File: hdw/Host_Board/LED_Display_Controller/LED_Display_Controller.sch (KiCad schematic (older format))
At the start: 0 parts

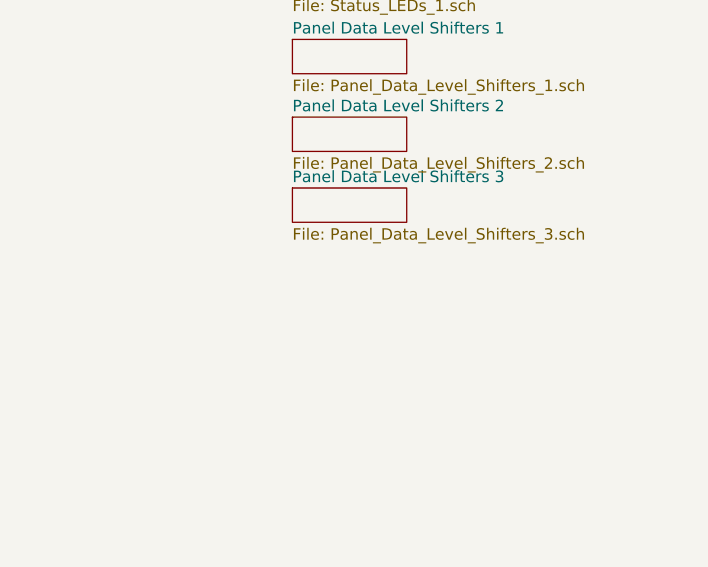
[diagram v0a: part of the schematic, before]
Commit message: Added test points sheet
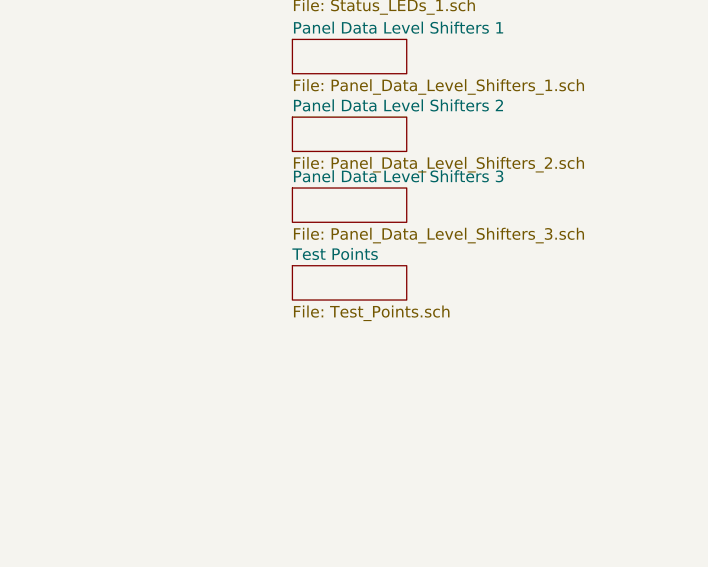
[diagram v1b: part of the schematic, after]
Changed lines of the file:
@@
 $Descr A 11000 8500
 encoding utf-8
-Sheet 1 25
+Sheet 1 26
 Title ""
 Date ""
@@
 Text Notes 710  7660 0    50   ~ 0
 To Do List:\n* Add +5V LED Power Supply (~~80 to 90A)\n* External oscillator for Micro?\n* Mechanical sheet\n* Design Power Input Circuit, add fusing\n* Decide on input power supply (AC/DC)\n* Add more power input connectors, match to AC/DC output connectors. Might need beefy Weurth shanks\n* Add status LEDs, PGOOD stuff\n* +3.3V Power Supply (~~2A)\n* +5V Monitoring/+3.3V Monitoring/Input Monitoring? Temperature sensors?\n* Add AUX +5V input if we mess up +5V supply\n* Wi-Fi Module\n* Evaluate Micro AVDD/AVSS filter\n* Select panel connector bulk caps, match with other tantalums on board for BOM scrubbing?\n* Power pushbutton? vs set on app?\n* Brightness encoder? vs set on app?\n* Add graphical items to certain sheets (ESD warning, heat, etc)\n* Add MU Logo to each sheet\n* Add Titles to each sheet\n* Add relevant design notes/routing notes to sheets\n* Add test points sheet\n* Re-order sheets\n* Wire everything to Micro\n* Assign Refdes's\n* Draw custom footprints\n* Assign footprints\n* Run ERC, resolve errors\n* Add firmware notes sheet\n* Add COM port settings note to USB sheet\n* Generate netlist\n* Generate BOM
+$Sheet
+S 7170 5330 500  150
+U 5BBF5233
+F0 "Test Points" 50
+F1 "Test_Points.sch" 50
+$EndSheet
 $EndSCHEMATC

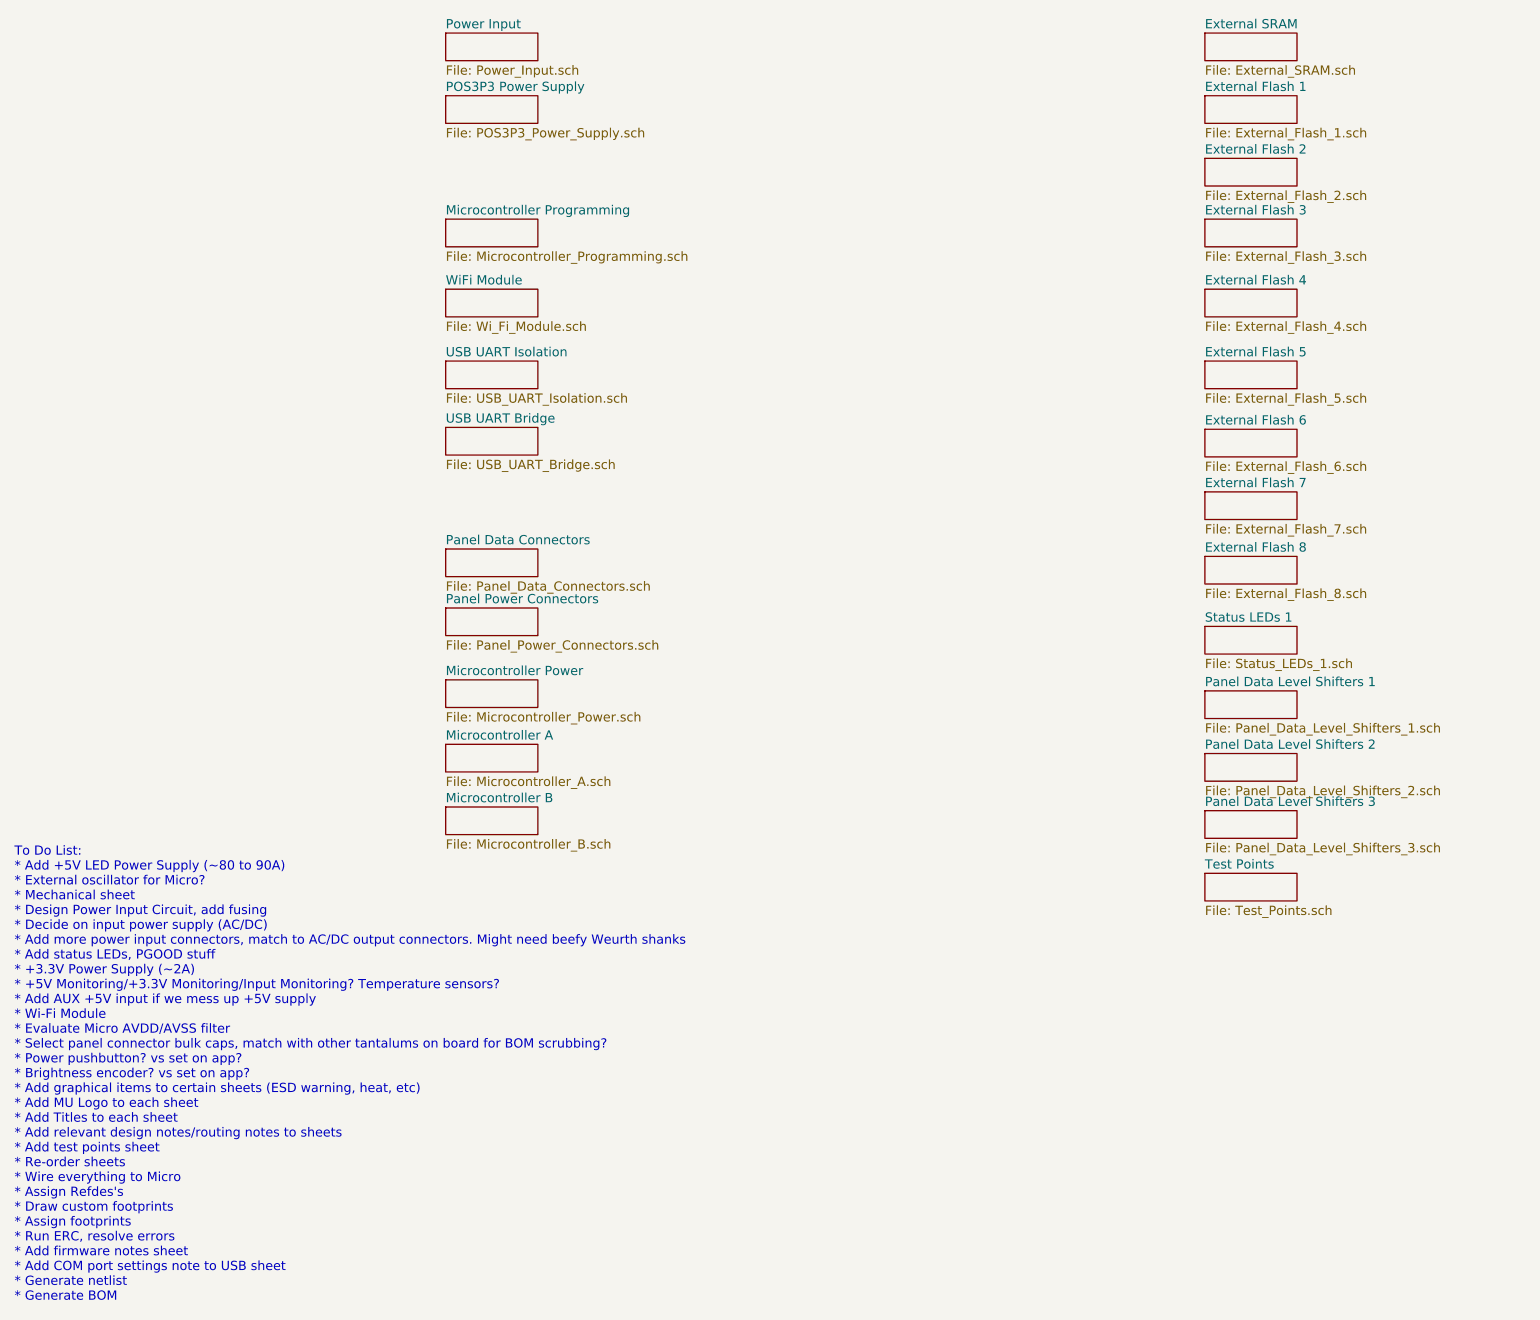
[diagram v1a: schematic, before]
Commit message: Added empty pages for POS5 Power supply
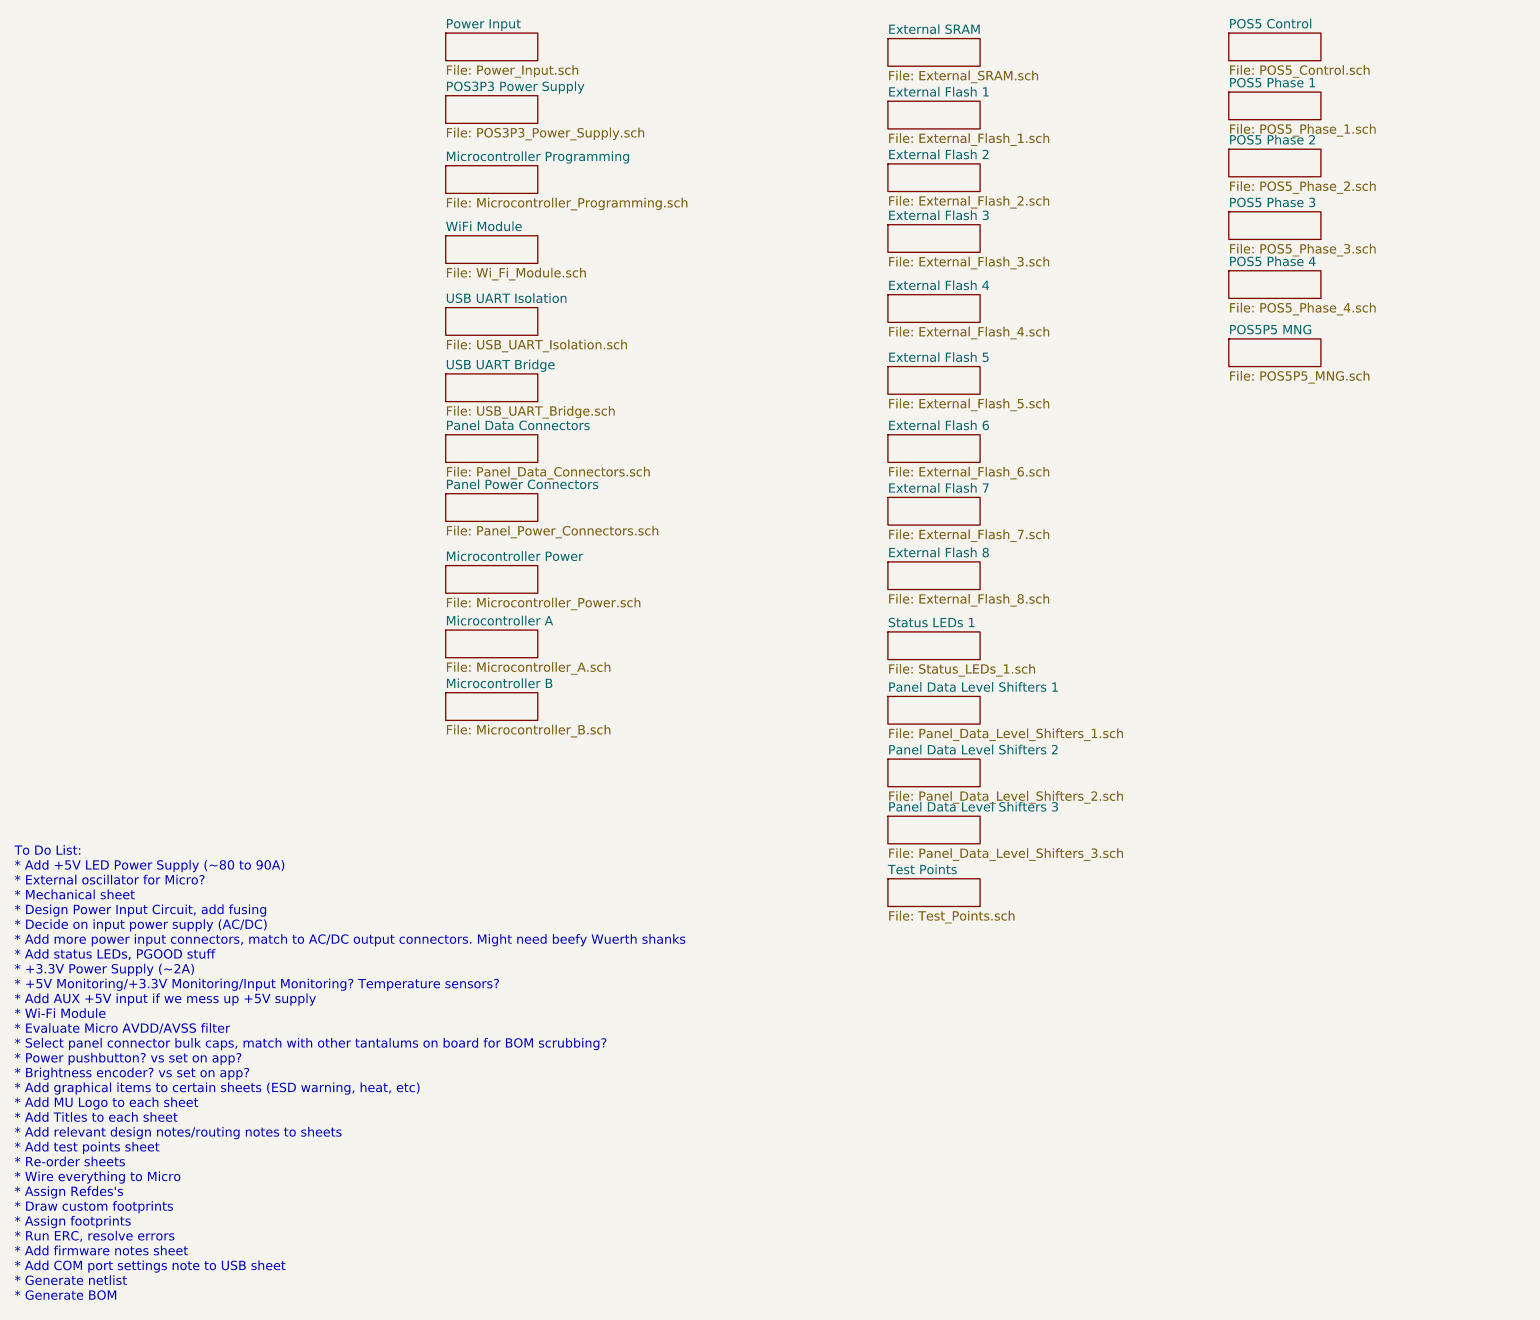
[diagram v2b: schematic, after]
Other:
- note added: "To Do List:\n* Add +5V LED Power Supply (~~80 to 90A)\n* External oscillator for Micro?\n* Mechanical sheet\n* Design Power Input Circuit, add fusing\n* Decide on input power supply (AC/DC)\n* Add more power input connectors, match to AC/DC output connectors. Might need beefy Wuerth shanks\n* Add status LEDs, PGOOD stuff\n* +3.3V Power Supply (~~2A)\n* +5V Monitoring/+3.3V Monitoring/Input Monito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"
- note removed: "To Do List:\n* Add +5V LED Power Supply (~~80 to 90A)\n* External oscillator for Micro?\n* Mechanical sheet\n* Design Power Input Circuit, add fusing\n* Decide on input power supply (AC/DC)\n* Add more power input connectors, match to AC/DC output connectors. Might need beefy Weurth shanks\n* Add status LEDs, PGOOD stuff\n* +3.3V Power Supply (~~2A)\n* +5V Monitoring/+3.3V Monitoring/Input Monito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"
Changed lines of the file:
@@
 $Descr A 11000 8500
 encoding utf-8
-Sheet 1 26
+Sheet 1 32
 Title ""
 Date ""
@@
 $EndSheet
 $Sheet
-S 3050 1780 500  150
+S 3050 1490 500  150
 U 5BAAE16C
 F0 "Microcontroller Programming" 50
@@
 $EndSheet
 $Sheet
-S 3050 2160 500  150
+S 3050 1870 500  150
 U 5BAAE1CB
 F0 "WiFi Module" 50
@@
 $EndSheet
 $Sheet
-S 3050 2550 500  150
+S 3050 2260 500  150
 U 5BAAE1DC
 F0 "USB UART Isolation" 50
@@
 $EndSheet
 $Sheet
-S 3050 2910 500  150
+S 3050 2620 500  150
 U 5BAAE1F3
 F0 "USB UART Bridge" 50
@@
 $EndSheet
 $Sheet
-S 3050 3570 500  150
+S 3050 2950 500  150
 U 5BAAE2CE
 F0 "Panel Data Connectors" 50
@@
 $EndSheet
 $Sheet
-S 3050 3890 500  150
+S 3050 3270 500  150
 U 5BAAE2DF
 F0 "Panel Power Connectors" 50
@@
 $EndSheet
 $Sheet
-S 3050 4280 500  150
+S 3050 3660 500  150
 U 5BB181D8
 F0 "Microcontroller Power" 50
@@
 $EndSheet
 $Sheet
-S 3050 4630 500  150
+S 3050 4010 500  150
 U 5BB182B1
 F0 "Microcontroller A" 50
@@
 $EndSheet
 $Sheet
-S 3050 4970 500  150
+S 3050 4350 500  150
 U 5BB1838A
 F0 "Microcontroller B" 50
@@
 $EndSheet
 $Sheet
-S 7170 770  500  150
+S 5450 800  500  150
 U 5BB2595B
 F0 "External SRAM" 50
@@
 $EndSheet
 $Sheet
-S 7170 1110 500  150
+S 5450 1140 500  150
 U 5BB2595E
 F0 "External Flash 1" 50
@@
 $EndSheet
 $Sheet
-S 7170 1450 500  150
+S 5450 1480 500  150
 U 5BB25AE7
 F0 "External Flash 2" 50
@@
 $EndSheet
 $Sheet
-S 7170 1780 500  150
+S 5450 1810 500  150
 U 5BB25AEA
 F0 "External Flash 3" 50
@@
 $EndSheet
 $Sheet
-S 7170 2160 500  150
+S 5450 2190 500  150
 U 5BB25AED
 F0 "External Flash 4" 50
@@
 $EndSheet
 $Sheet
-S 7170 2550 500  150
+S 5450 2580 500  150
 U 5BB25AF0
 F0 "External Flash 5" 50
@@
 $EndSheet
 $Sheet
-S 7170 2920 500  150
+S 5450 2950 500  150
 U 5BB53D61
 F0 "External Flash 6" 50
@@
 $EndSheet
 $Sheet
-S 7170 3260 500  150
+S 5450 3290 500  150
 U 5BB53D64
 F0 "External Flash 7" 50
@@
 $EndSheet
 $Sheet
-S 7170 3610 500  150
+S 5450 3640 500  150
 U 5BB53D67
 F0 "External Flash 8" 50
@@
 $EndSheet
 $Sheet
-S 7170 3990 500  150
+S 5450 4020 500  150
 U 5BB844FD
 F0 "Status LEDs 1" 50
@@
 $EndSheet
 $Sheet
-S 7170 4340 500  150
+S 5450 4370 500  150
 U 5BBE424C
 F0 "Panel Data Level Shifters 1" 50
@@
 $EndSheet
 $Sheet
-S 7170 4680 500  150
+S 5450 4710 500  150
 U 5BBE424F
 F0 "Panel Data Level Shifters 2" 50
@@
 $EndSheet
 $Sheet
-S 7170 4990 500  150
+S 5450 5020 500  150
 U 5BBE4252
 F0 "Panel Data Level Shifters 3" 50
@@
 $EndSheet
 Text Notes 710  7660 0    50   ~ 0
-To Do List:\n* Add +5V LED Power Supply (~~80 to 90A)\n* External oscillator for Micro?\n* Mechanical sheet\n* Design Power Input Circuit, add fusing\n* Decide on input power supply (AC/DC)\n* Add more power input connectors, match to AC/DC output connectors. Might need beefy Weurth shanks\n* Add status LEDs, PGOOD stuff\n* +3.3V Power Supply (~~2A)\n* +5V Monitoring/+3.3V Monitoring/Input Monitoring? Temperature sensors?\n* Add AUX +5V input if we mess up +5V supply\n* Wi-Fi Module\n* Evaluate Micro AVDD/AVSS filter\n* Select panel connector bulk caps, match with other tantalums on board for BOM scrubbing?\n* Power pushbutton? vs set on app?\n* Brightness encoder? vs set on app?\n* Add graphical items to certain sheets (ESD warning, heat, etc)\n* Add MU Logo to each sheet\n* Add Titles to each sheet\n* Add relevant design notes/routing notes to sheets\n* Add test points sheet\n* Re-order sheets\n* Wire everything to Micro\n* Assign Refdes's\n* Draw custom footprints\n* Assign footprints\n* Run ERC, resolve errors\n* Add firmware notes sheet\n* Add COM port settings note to USB sheet\n* Generate netlist\n* Generate BOM
-$Sheet
-S 7170 5330 500  150
+To Do List:\n* Add +5V LED Power Supply (~~80 to 90A)\n* External oscillator for Micro?\n* Mechanical sheet\n* Design Power Input Circuit, add fusing\n* Decide on input power supply (AC/DC)\n* Add more power input connectors, match to AC/DC output connectors. Might need beefy Wuerth shanks\n* Add status LEDs, PGOOD stuff\n* +3.3V Power Supply (~~2A)\n* +5V Monitoring/+3.3V Monitoring/Input Monitoring? Temperature sensors?\n* Add AUX +5V input if we mess up +5V supply\n* Wi-Fi Module\n* Evaluate Micro AVDD/AVSS filter\n* Select panel connector bulk caps, match with other tantalums on board for BOM scrubbing?\n* Power pushbutton? vs set on app?\n* Brightness encoder? vs set on app?\n* Add graphical items to certain sheets (ESD warning, heat, etc)\n* Add MU Logo to each sheet\n* Add Titles to each sheet\n* Add relevant design notes/routing notes to sheets\n* Add test points sheet\n* Re-order sheets\n* Wire everything to Micro\n* Assign Refdes's\n* Draw custom footprints\n* Assign footprints\n* Run ERC, resolve errors\n* Add firmware notes sheet\n* Add COM port settings note to USB sheet\n* Generate netlist\n* Generate BOM
+$Sheet
+S 5450 5360 500  150
 U 5BBF5233
 F0 "Test Points" 50
 F1 "Test_Points.sch" 50
 $EndSheet
+$Sheet
+S 7300 770  500  150
+U 5BC2370E
+F0 "POS5 Control" 50
+F1 "POS5_Control.sch" 50
+$EndSheet
+$Sheet
+S 7300 1090 500  150
+U 5BC23711
+F0 "POS5 Phase 1" 50
+F1 "POS5_Phase_1.sch" 50
+$EndSheet
+$Sheet
+S 7300 1400 500  150
+U 5BC23715
+F0 "POS5 Phase 2" 50
+F1 "POS5_Phase_2.sch" 50
+$EndSheet
+$Sheet
+S 7300 1740 500  150
+U 5BC2371A
+F0 "POS5 Phase 3" 50
+F1 "POS5_Phase_3.sch" 50
+$EndSheet
+$Sheet
+S 7300 2060 500  150
+U 5BC2371D
+F0 "POS5 Phase 4" 50
+F1 "POS5_Phase_4.sch" 50
+$EndSheet
+$Sheet
+S 7300 2430 500  150
+U 5BC23720
+F0 "POS5P5 MNG" 50
+F1 "POS5P5_MNG.sch" 50
+$EndSheet
 $EndSCHEMATC

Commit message: Overriding master branch for clean pull request
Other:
- note added: "To Do List:\n* Mechanical sheet\n* Decide on input power supply (AC/DC)\n* Add more power input connectors, match to AC/DC output connectors. Might need beefy Wuerth shanks\n* Add status LEDs, PGOOD stuff\n* +3.3V Power Supply (~~2A)\n* Add AUX +5V input if we mess up +5V supply\n* Wi-Fi Module\n* Evaluate Micro AVDD/AVSS filter\n* Power pushbutton? vs set on app?\n* Brightness encoder? vs set on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"
- note removed: "To Do List:\n* Add +5V LED Power Supply (~~80 to 90A)\n* External oscillator for Micro?\n* Mechanical sheet\n* Design Power Input Circuit, add fusing\n* Decide on input power supply (AC/DC)\n* Add more power input connectors, match to AC/DC output connectors. Might need beefy Wuerth shanks\n* Add status LEDs, PGOOD stuff\n* +3.3V Power Supply (~~2A)\n* +5V Monitoring/+3.3V Monitoring/Input Monito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"
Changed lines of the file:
@@
 $EndSheet
 Text Notes 710  7660 0    50   ~ 0
-To Do List:\n* Add +5V LED Power Supply (~~80 to 90A)\n* External oscillator for Micro?\n* Mechanical sheet\n* Design Power Input Circuit, add fusing\n* Decide on input power supply (AC/DC)\n* Add more power input connectors, match to AC/DC output connectors. Might need beefy Wuerth shanks\n* Add status LEDs, PGOOD stuff\n* +3.3V Power Supply (~~2A)\n* +5V Monitoring/+3.3V Monitoring/Input Monitoring? Temperature sensors?\n* Add AUX +5V input if we mess up +5V supply\n* Wi-Fi Module\n* Evaluate Micro AVDD/AVSS filter\n* Select panel connector bulk caps, match with other tantalums on board for BOM scrubbing?\n* Power pushbutton? vs set on app?\n* Brightness encoder? vs set on app?\n* Add graphical items to certain sheets (ESD warning, heat, etc)\n* Add MU Logo to each sheet\n* Add Titles to each sheet\n* Add relevant design notes/routing notes to sheets\n* Add test points sheet\n* Re-order sheets\n* Wire everything to Micro\n* Assign Refdes's\n* Draw custom footprints\n* Assign footprints\n* Run ERC, resolve errors\n* Add firmware notes sheet\n* Add COM port settings note to USB sheet\n* Generate netlist\n* Generate BOM
+To Do List:\n* Mechanical sheet\n* Decide on input power supply (AC/DC)\n* Add more power input connectors, match to AC/DC output connectors. Might need beefy Wuerth shanks\n* Add status LEDs, PGOOD stuff\n* +3.3V Power Supply (~~2A)\n* Add AUX +5V input if we mess up +5V supply\n* Wi-Fi Module\n* Evaluate Micro AVDD/AVSS filter\n* Power pushbutton? vs set on app?\n* Brightness encoder? vs set on app?\n* Add graphical items to certain sheets (ESD warning, heat, etc)\n* Add MU Logo to each sheet\n* Add Titles to each sheet\n* Add relevant design notes/routing notes to sheets\n* Add test points sheet\n* Re-order sheets\n* Wire everything to Micro\n* Assign Refdes's\n* Draw custom footprints\n* Assign footprints\n* Run ERC, resolve errors\n* Add firmware notes sheet\n* Add COM port settings note to USB sheet\n* Generate netlist\n* Generate BOM
 $Sheet
 S 5450 5360 500  150
